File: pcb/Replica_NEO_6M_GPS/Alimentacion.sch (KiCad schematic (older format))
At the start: 7 parts, among them U1 TPS79133DBVR

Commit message: se hicieron correcciones
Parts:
- U1: footprint SOT95P280X145-5N -> TPS79133DBVR:SOT95P280X145-5N
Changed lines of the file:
@@
 Title "Regulador 3.3V"
 Date "2021-07-12"
-Rev ""
+Rev "1.0"
 Comp "Christian Canaan Castro Botek UBA - Argentina"
 Comment1 ""
@@
 F 0 "U1" H 5550 4020 50  0000 C CNN
 F 1 "TPS79133DBVR" H 5550 3929 50  0000 C CNN
-F 2 "SOT95P280X145-5N" H 5550 3450 50  0001 L BNN
+F 2 "TPS79133DBVR:SOT95P280X145-5N" H 5550 3450 50  0001 L BNN
 F 3 "" H 5550 3450 50  0001 L BNN
 	1    5550 3450

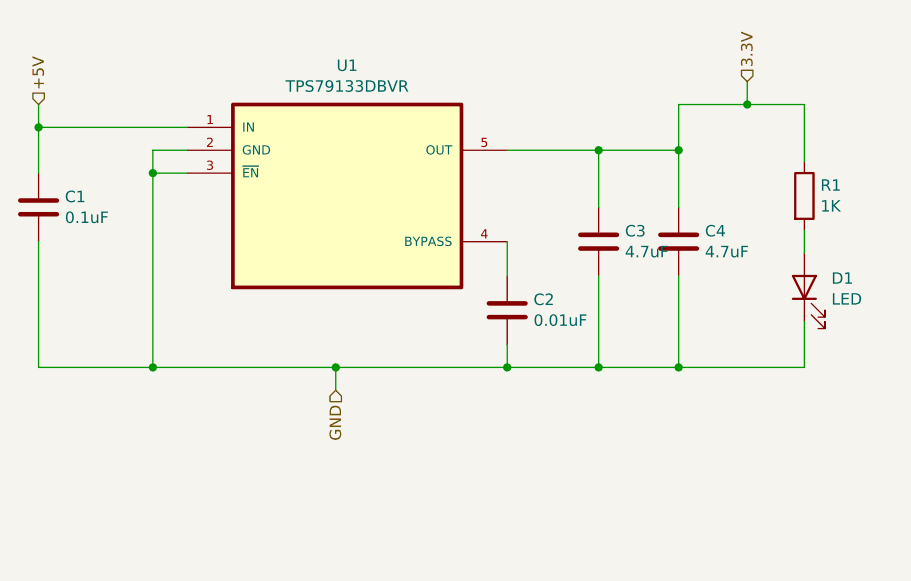
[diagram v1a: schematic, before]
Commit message: Se agregaron footprints y se hicieron correcciones menores
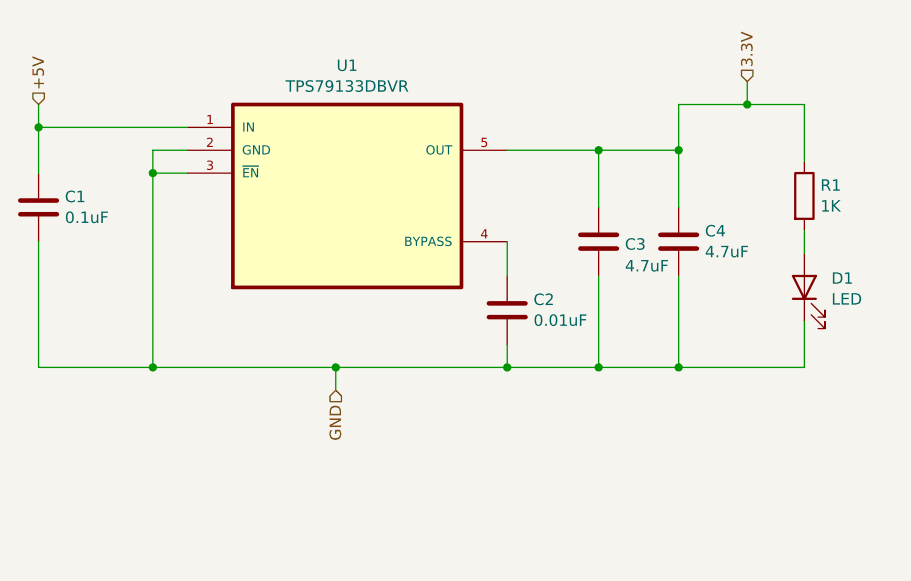
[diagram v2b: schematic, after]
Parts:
- C1, C2, C3, C4: footprint (none) -> Capacitor_SMD:C_0805_2012Metric_Pad1.18x1.45mm_HandSolder
- D1: footprint (none) -> LED_SMD:LED_0201_0603Metric_Pad0.64x0.40mm_HandSolder
- R1: footprint (none) -> Resistor_SMD:R_0805_2012Metric_Pad1.20x1.40mm_HandSolder
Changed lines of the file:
@@
 F 0 "C1" H 4315 3546 50  0000 L CNN
 F 1 "0.1uF" H 4315 3455 50  0000 L CNN
-F 2 "" H 4238 3350 50  0001 C CNN
+F 2 "Capacitor_SMD:C_0805_2012Metric_Pad1.18x1.45mm_HandSolder" H 4238 3350 50  0001 C CNN
 F 3 "~" H 4200 3500 50  0001 C CNN
 	1    4200 3500
@@
 F 0 "C2" H 6365 3996 50  0000 L CNN
 F 1 "0.01uF" H 6365 3905 50  0000 L CNN
-F 2 "" H 6288 3800 50  0001 C CNN
+F 2 "Capacitor_SMD:C_0805_2012Metric_Pad1.18x1.45mm_HandSolder" H 6288 3800 50  0001 C CNN
 F 3 "~" H 6250 3950 50  0001 C CNN
 	1    6250 3950
@@
 U 1 1 60ECD2B3
 P 6650 3650
-F 0 "C3" H 6765 3696 50  0000 L CNN
-F 1 "4.7uF" H 6765 3605 50  0000 L CNN
-F 2 "" H 6688 3500 50  0001 C CNN
+F 0 "C3" H 6765 3638 50  0000 L CNN
+F 1 "4.7uF" H 6765 3543 50  0000 L CNN
+F 2 "Capacitor_SMD:C_0805_2012Metric_Pad1.18x1.45mm_HandSolder" H 6688 3500 50  0001 C CNN
 F 3 "~" H 6650 3650 50  0001 C CNN
 	1    6650 3650
@@
 F 0 "C4" H 7115 3696 50  0000 L CNN
 F 1 "4.7uF" H 7115 3605 50  0000 L CNN
-F 2 "" H 7038 3500 50  0001 C CNN
+F 2 "Capacitor_SMD:C_0805_2012Metric_Pad1.18x1.45mm_HandSolder" H 7038 3500 50  0001 C CNN
 F 3 "~" H 7000 3650 50  0001 C CNN
 	1    7000 3650
@@
 F 0 "R1" H 7620 3496 50  0000 L CNN
 F 1 "1K" H 7620 3405 50  0000 L CNN
-F 2 "" V 7480 3450 50  0001 C CNN
+F 2 "Resistor_SMD:R_0805_2012Metric_Pad1.20x1.40mm_HandSolder" V 7480 3450 50  0001 C CNN
 F 3 "~" H 7550 3450 50  0001 C CNN
 	1    7550 3450
@@
 F 0 "D1" V 7589 3732 50  0000 R CNN
 F 1 "LED" V 7498 3732 50  0000 R CNN
-F 2 "" H 7550 3850 50  0001 C CNN
+F 2 "LED_SMD:LED_0201_0603Metric_Pad0.64x0.40mm_HandSolder" H 7550 3850 50  0001 C CNN
 F 3 "~" H 7550 3850 50  0001 C CNN
 	1    7550 3850

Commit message: Se hicieron correcciones y se avanzo con el PCB
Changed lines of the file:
@@
 	4700 3350 4700 4200
-Wire Wire Line
-	4850 3150 4200 3150
 Wire Wire Line
 	4200 3150 4200 3350
@@
 Wire Wire Line
 	5500 4200 6250 4200
+Wire Wire Line
+	4200 3150 4850 3150
 $EndSCHEMATC

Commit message: Se hicieron cambiaron los footprints de los LEDS D1,D2
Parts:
- D1: footprint LED_SMD:LED_0201_0603Metric_Pad0.64x0.40mm_HandSolder -> LED_SMD:LED_0805_2012Metric_Pad1.15x1.40mm_HandSolder
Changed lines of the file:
@@
 F 0 "D1" V 7589 3732 50  0000 R CNN
 F 1 "LED" V 7498 3732 50  0000 R CNN
-F 2 "LED_SMD:LED_0201_0603Metric_Pad0.64x0.40mm_HandSolder" H 7550 3850 50  0001 C CNN
+F 2 "LED_SMD:LED_0805_2012Metric_Pad1.15x1.40mm_HandSolder" H 7550 3850 50  0001 C CNN
 F 3 "~" H 7550 3850 50  0001 C CNN
 	1    7550 3850

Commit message: Se acomodaron archivos y se hicieron retoques
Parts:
- U1: symbol TPS79133DBVR:TPS79133DBVR -> Replica_NEO_6M_GPS-rescue:TPS79133DBVR-TPS79133DBVR
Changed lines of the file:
@@
 $EndDescr
 $Comp
-L TPS79133DBVR:TPS79133DBVR U1
+L Replica_NEO_6M_GPS-rescue:TPS79133DBVR-TPS79133DBVR U1
 U 1 1 60ECBB96
 P 5550 3450

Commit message: se retoco el esquematico
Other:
- moved on the sheet: C1, C2, C3, C4, D1, R1, U1
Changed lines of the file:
@@
 L Replica_NEO_6M_GPS-rescue:TPS79133DBVR-TPS79133DBVR U1
 U 1 1 60ECBB96
-P 5550 3450
-F 0 "U1" H 5550 4020 50  0000 C CNN
-F 1 "TPS79133DBVR" H 5550 3929 50  0000 C CNN
-F 2 "TPS79133DBVR:SOT95P280X145-5N" H 5550 3450 50  0001 L BNN
-F 3 "" H 5550 3450 50  0001 L BNN
-	1    5550 3450
+P 5650 3950
+F 0 "U1" H 5650 4520 50  0000 C CNN
+F 1 "TPS79133DBVR" H 5650 4429 50  0000 C CNN
+F 2 "TPS79133DBVR:SOT95P280X145-5N" H 5650 3950 50  0001 L BNN
+F 3 "" H 5650 3950 50  0001 L BNN
+	1    5650 3950
 	1    0    0    -1
 $EndComp
@@
 L Device:C C1
 U 1 1 60ECC43D
-P 4200 3500
-F 0 "C1" H 4315 3546 50  0000 L CNN
-F 1 "0.1uF" H 4315 3455 50  0000 L CNN
-F 2 "Capacitor_SMD:C_0805_2012Metric_Pad1.18x1.45mm_HandSolder" H 4238 3350 50  0001 C CNN
-F 3 "~" H 4200 3500 50  0001 C CNN
-	1    4200 3500
+P 4300 4000
+F 0 "C1" H 4415 4046 50  0000 L CNN
+F 1 "0.1uF" H 4415 3955 50  0000 L CNN
+F 2 "Capacitor_SMD:C_0805_2012Metric_Pad1.18x1.45mm_HandSolder" H 4338 3850 50  0001 C CNN
+F 3 "~" H 4300 4000 50  0001 C CNN
+	1    4300 4000
 	1    0    0    -1
 $EndComp
@@
 L Device:C C2
 U 1 1 60ECCA14
-P 6250 3950
-F 0 "C2" H 6365 3996 50  0000 L CNN
-F 1 "0.01uF" H 6365 3905 50  0000 L CNN
-F 2 "Capacitor_SMD:C_0805_2012Metric_Pad1.18x1.45mm_HandSolder" H 6288 3800 50  0001 C CNN
-F 3 "~" H 6250 3950 50  0001 C CNN
-	1    6250 3950
+P 6350 4450
+F 0 "C2" H 6465 4496 50  0000 L CNN
+F 1 "0.01uF" H 6465 4405 50  0000 L CNN
+F 2 "Capacitor_SMD:C_0805_2012Metric_Pad1.18x1.45mm_HandSolder" H 6388 4300 50  0001 C CNN
+F 3 "~" H 6350 4450 50  0001 C CNN
+	1    6350 4450
 	1    0    0    -1
 $EndComp
@@
 L Device:C C3
 U 1 1 60ECD2B3
-P 6650 3650
-F 0 "C3" H 6765 3638 50  0000 L CNN
-F 1 "4.7uF" H 6765 3543 50  0000 L CNN
-F 2 "Capacitor_SMD:C_0805_2012Metric_Pad1.18x1.45mm_HandSolder" H 6688 3500 50  0001 C CNN
-F 3 "~" H 6650 3650 50  0001 C CNN
-	1    6650 3650
+P 6750 4150
+F 0 "C3" H 6865 4138 50  0000 L CNN
+F 1 "4.7uF" H 6865 4043 50  0000 L CNN
+F 2 "Capacitor_SMD:C_0805_2012Metric_Pad1.18x1.45mm_HandSolder" H 6788 4000 50  0001 C CNN
+F 3 "~" H 6750 4150 50  0001 C CNN
+	1    6750 4150
 	1    0    0    -1
 $EndComp
@@
 L Device:C C4
 U 1 1 60ECD89A
-P 7000 3650
-F 0 "C4" H 7115 3696 50  0000 L CNN
-F 1 "4.7uF" H 7115 3605 50  0000 L CNN
-F 2 "Capacitor_SMD:C_0805_2012Metric_Pad1.18x1.45mm_HandSolder" H 7038 3500 50  0001 C CNN
-F 3 "~" H 7000 3650 50  0001 C CNN
-	1    7000 3650
+P 7100 4150
+F 0 "C4" H 7215 4196 50  0000 L CNN
+F 1 "4.7uF" H 7215 4105 50  0000 L CNN
+F 2 "Capacitor_SMD:C_0805_2012Metric_Pad1.18x1.45mm_HandSolder" H 7138 4000 50  0001 C CNN
+F 3 "~" H 7100 4150 50  0001 C CNN
+	1    7100 4150
 	1    0    0    -1
 $EndComp
@@
 L Device:R R1
 U 1 1 60ED22D6
-P 7550 3450
-F 0 "R1" H 7620 3496 50  0000 L CNN
-F 1 "1K" H 7620 3405 50  0000 L CNN
-F 2 "Resistor_SMD:R_0805_2012Metric_Pad1.20x1.40mm_HandSolder" V 7480 3450 50  0001 C CNN
-F 3 "~" H 7550 3450 50  0001 C CNN
-	1    7550 3450
+P 7650 3950
+F 0 "R1" H 7720 3996 50  0000 L CNN
+F 1 "1K" H 7720 3905 50  0000 L CNN
+F 2 "Resistor_SMD:R_0805_2012Metric_Pad1.20x1.40mm_HandSolder" V 7580 3950 50  0001 C CNN
+F 3 "~" H 7650 3950 50  0001 C CNN
+	1    7650 3950
 	1    0    0    -1
 $EndComp
@@
 L Device:LED D1
 U 1 1 60ED357F
-P 7550 3850
-F 0 "D1" V 7589 3732 50  0000 R CNN
-F 1 "LED" V 7498 3732 50  0000 R CNN
-F 2 "LED_SMD:LED_0805_2012Metric_Pad1.15x1.40mm_HandSolder" H 7550 3850 50  0001 C CNN
-F 3 "~" H 7550 3850 50  0001 C CNN
-	1    7550 3850
+P 7650 4350
+F 0 "D1" V 7689 4232 50  0000 R CNN
+F 1 "LED" V 7598 4232 50  0000 R CNN
+F 2 "LED_SMD:LED_0805_2012Metric_Pad1.15x1.40mm_HandSolder" H 7650 4350 50  0001 C CNN
+F 3 "~" H 7650 4350 50  0001 C CNN
+	1    7650 4350
 	0    -1   -1   0
 $EndComp
 Wire Wire Line
-	6250 3250 6650 3250
+	6350 3750 6750 3750
 Wire Wire Line
-	7000 3250 7000 3500
+	7100 3750 7100 4000
 Wire Wire Line
-	6650 3250 6650 3500
-Connection ~ 6650 3250
+	6750 3750 6750 4000
+Connection ~ 6750 3750
 Wire Wire Line
-	6650 3250 7000 3250
+	6750 3750 7100 3750
 Wire Wire Line
-	6250 3650 6250 3800
+	6350 4150 6350 4300
 Wire Wire Line
-	6250 4100 6250 4200
+	6350 4600 6350 4700
 Wire Wire Line
-	6650 3800 6650 4200
+	6750 4300 6750 4700
 Wire Wire Line
-	7000 3800 7000 4200
+	7100 4300 7100 4700
 Wire Wire Line
-	7550 3600 7550 3700
+	7650 4100 7650 4200
 Wire Wire Line
-	7550 4000 7550 4200
+	7650 4500 7650 4700
 Wire Wire Line
-	4850 3250 4700 3250
+	4950 3750 4800 3750
 Wire Wire Line
-	4700 3250 4700 3350
+	4800 3750 4800 3850
 Wire Wire Line
-	4850 3350 4700 3350
-Connection ~ 4700 3350
+	4950 3850 4800 3850
+Connection ~ 4800 3850
 Wire Wire Line
-	4700 3350 4700 4200
+	4800 3850 4800 4700
 Wire Wire Line
-	4200 3150 4200 3350
+	4300 3650 4300 3850
 Wire Wire Line
-	4200 3650 4200 4200
+	4300 4150 4300 4700
 Wire Wire Line
-	7550 3050 7550 3300
+	7650 3550 7650 3800
 Wire Wire Line
-	7000 3050 7000 3250
-Connection ~ 7000 3250
+	7100 3550 7100 3750
+Connection ~ 7100 3750
 Wire Wire Line
-	4200 3050 4200 3150
-Connection ~ 4200 3150
-Text HLabel 7300 2950 1    50   Input ~ 0
+	4300 3550 4300 3650
+Connection ~ 4300 3650
+Text HLabel 7400 3450 1    50   Input ~ 0
 3.3V
 Wire Wire Line
-	7000 3050 7300 3050
+	7100 3550 7400 3550
 Wire Wire Line
-	7300 3050 7300 2950
-Connection ~ 7300 3050
+	7400 3550 7400 3450
+Connection ~ 7400 3550
 Wire Wire Line
-	7300 3050 7550 3050
-Text HLabel 4200 3050 1    50   Input ~ 0
+	7400 3550 7650 3550
+Text HLabel 4300 3550 1    50   Input ~ 0
 +5V
-Text HLabel 5500 4300 3    50   Input ~ 0
+Text HLabel 5600 4800 3    50   Input ~ 0
 GND
 Wire Wire Line
-	4200 4200 4700 4200
+	4300 4700 4800 4700
 Wire Wire Line
-	4700 4200 5500 4200
-Connection ~ 4700 4200
+	4800 4700 5600 4700
+Connection ~ 4800 4700
 Wire Wire Line
-	6250 4200 6650 4200
-Connection ~ 6250 4200
+	6350 4700 6750 4700
+Connection ~ 6350 4700
 Wire Wire Line
-	6650 4200 7000 4200
-Connection ~ 6650 4200
+	6750 4700 7100 4700
+Connection ~ 6750 4700
 Wire Wire Line
-	7000 4200 7550 4200
-Connection ~ 7000 4200
+	7100 4700 7650 4700
+Connection ~ 7100 4700
 Wire Wire Line
-	5500 4300 5500 4200
-Connection ~ 5500 4200
+	5600 4800 5600 4700
+Connection ~ 5600 4700
 Wire Wire Line
-	5500 4200 6250 4200
+	5600 4700 6350 4700
 Wire Wire Line
-	4200 3150 4850 3150
+	4300 3650 4950 3650
 $EndSCHEMATC
